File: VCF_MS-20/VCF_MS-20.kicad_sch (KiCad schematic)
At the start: 42 parts, among them J1 POWER, J2 AUDIO IN, J3 AUDIO OUT, J4 CV IN, Q1 BC558, Q2 BC558, SW1/HPLP1 SW_DPDT_x2, SW2/OCT1 SW_SPDT/ATT, U1 LM324, U2 LM13700

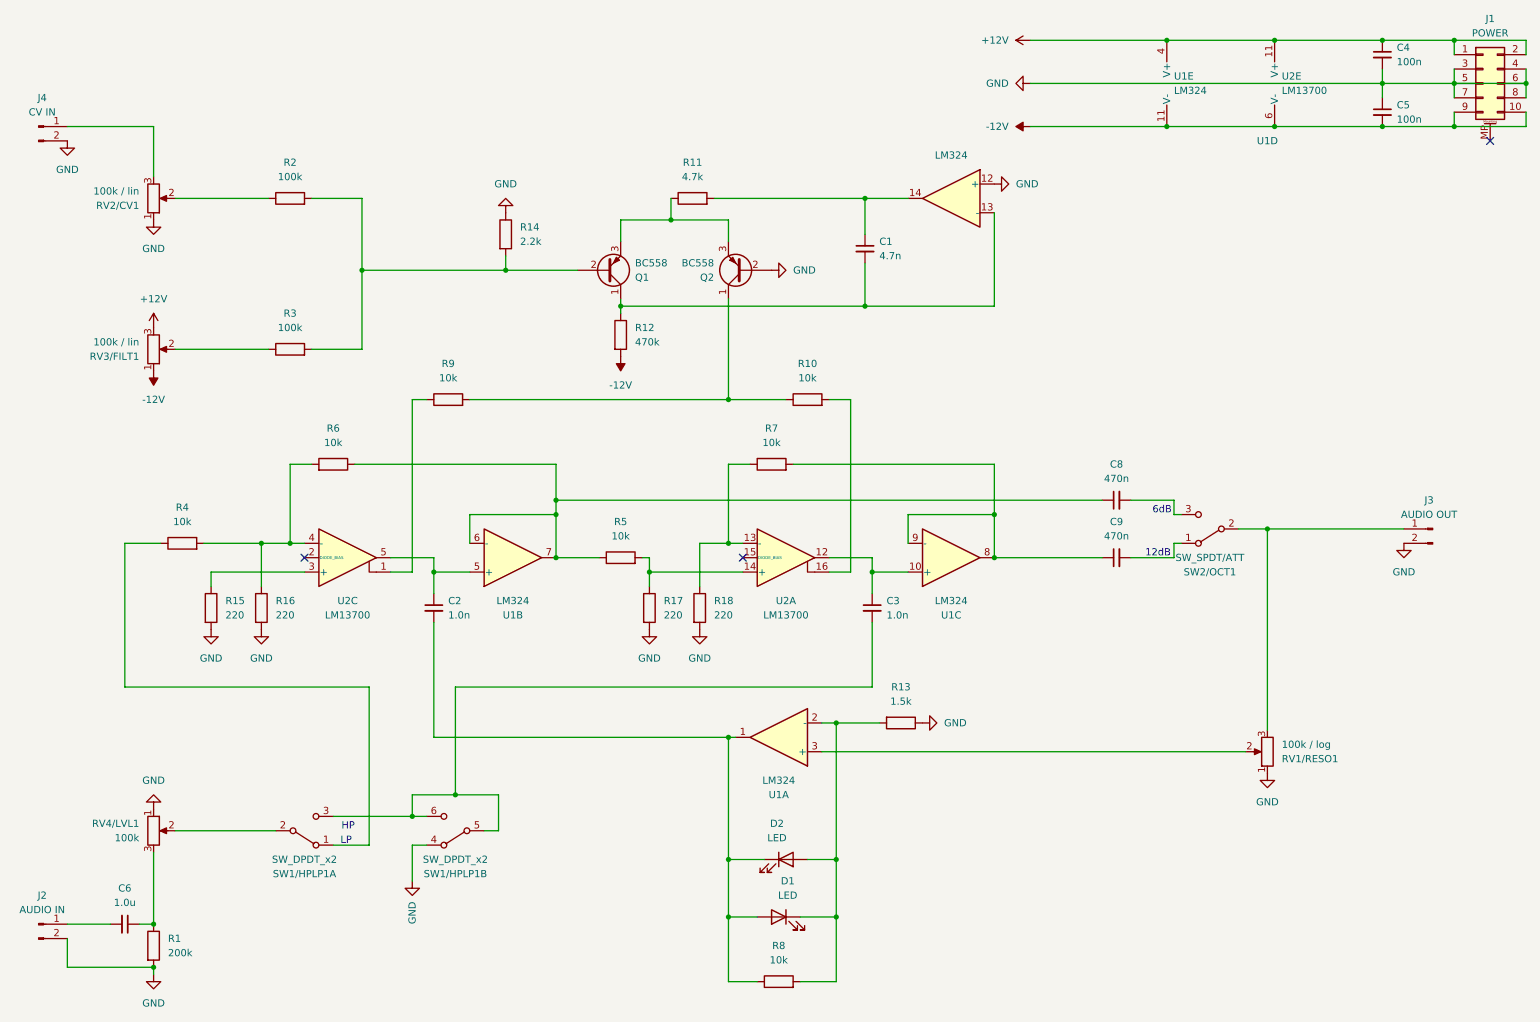
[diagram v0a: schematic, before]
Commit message: Update MS-20 VCO
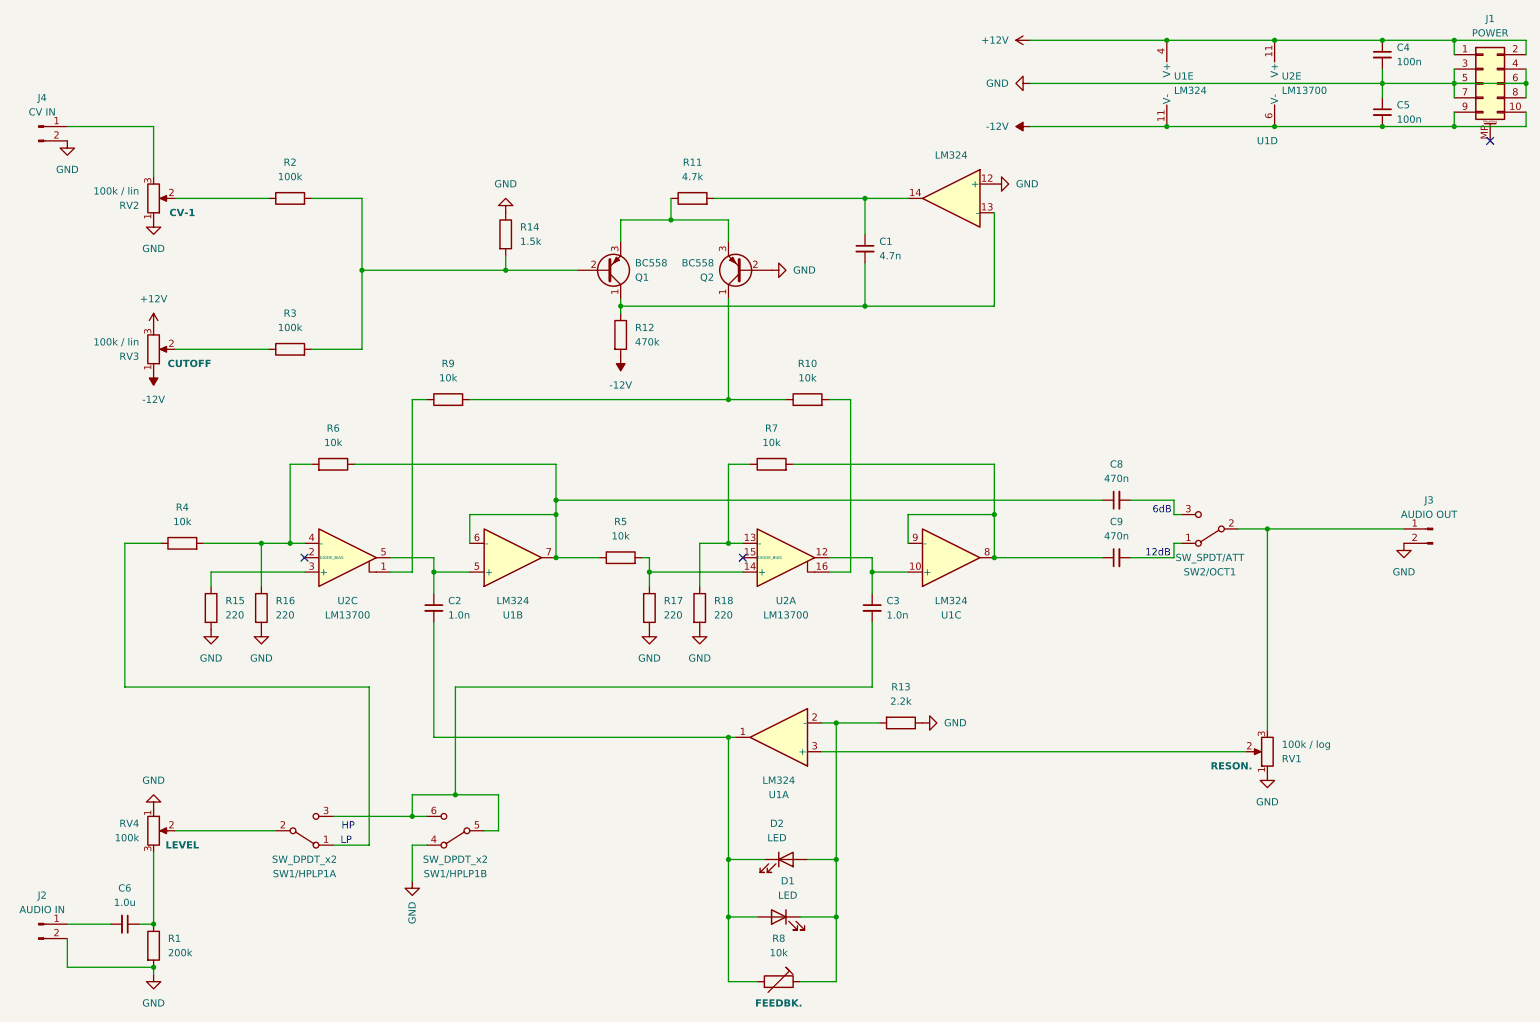
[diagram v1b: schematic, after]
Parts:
- removed R8: 10k, Resistor_THT:R_Axial_DIN0207_L6.3mm_D2.5mm_P15.24mm_Horizontal, symbol Device:R
- added R8: 10k, symbol Device:R_Trim
- R13: value 1.5k -> 2.2k
- R14: value 2.2k -> 1.5k
- RV1: renamed from RV1/RESO1; Note (none) -> RESON.
- RV2: renamed from RV2/CV1; Note (none) -> CV-1
- RV3: renamed from RV3/FILT1; Note (none) -> CUTOFF
- RV4: renamed from RV4/LVL1; Note (none) -> LEVEL
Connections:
- net at C2.2, D1.2 (A), D2.1 (K)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: now also R8.2
- net at D1.1 (K), D2.2 (A), R13.2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: now also R8.1
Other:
- title: (none) -> Late MS-20 VCO / Eurorack

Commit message: Update pcb
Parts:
- removed C9: 470n, Capacitor_THT:C_Disc_D7.5mm_W2.5mm_P5.00mm, symbol Device:C_Small
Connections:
- net at J3.1 (Pin_1), RV1.3: now also C8.2; no longer SW2/OCT1.2 (B)
- net at R7.2, U1.8, U1.9 (-): now also SW2/OCT1.1 (A)
- net at C2.2, D1.2 (A), D2.1 (K)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: now also R8.1; no longer R8.2
- net at D1.1 (K), D2.2 (A), R13.2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: now also R8.2; no longer R8.1
- net at SW2/OCT1.3 (C): now also R5.1, R6.1, U1.6 (-), U1.7; no longer C8.2
- new net: C8.1, SW2/OCT1.2 (B)
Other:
- moved on the sheet: C8, J3, R8, SW2/OCT1

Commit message: Update pcb
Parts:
- C1: Code (none) -> 472
- C2, C3: Code (none) -> 105Z
- R10, R4, R5, R6, R7, R8, R9: Code (none) -> br-bk-or-gd
- R11: Code (none) -> yw-pu-rd-gd
- R12: Code (none) -> yw-pu-yw-gd
- R13: Code (none) -> rd-rd-rd-gd
- R14: Code (none) -> br-gr-rd-gd
- R15, R16, R17, R18: Code (none) -> rd-rd-br-gd
- R2, R3: Code (none) -> br-bk-yw-gd
